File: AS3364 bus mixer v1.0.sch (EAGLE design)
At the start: 62 parts, among them IC1 TL072JD, IC2 TL072JD, IC3 TL072JD, IC30 TL072JT, IC4 TL072JD, IC5 79L09F, IC6 78L09F, IC7 CH446Q

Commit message: Tracing the bus mixer
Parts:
- removed SV1: (no value), joakim:MA15-1JP
- added +12V, -12V, BC_IN, BUS_A, BUS_B, CS/CK, CV1, CV2, CV3, CV4, CV5, CV6, CV7, CV8, DAT, DIST_IN, FX_A, FX_B, GND, IN1, IN2, IN3, IN4, IN5, IN6, IN7, IN8, RST, STB: (no value), joakim:MA01-1JN8MM
- IC1, IC2, IC3, IC4: value TL072JD -> TL072JT; device joakim:TL072JD -> joakim:TL072JT
- R14, R15, R16, R17, R31, R32, R33, R34, R47, R48: device rcl:R-EU_R0603 -> rcl:R-EU_R0402
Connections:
- new net BITCRUSH_IN: BC_IN.1, IC7.Y5
- new net CS/CK: CS/CK.1, IC7.CS/CK
- new net CV5: CV5.1, R19.1
- new net CV6: CV6.1, R20.1
- new net CV6_IN: DA1G$1.CV1, R20.2, R28.2
- new net CV7: CV7.1, R18.1
- new net CV8: CV8.1, R21.1
- new net DAT: DAT.1, IC7.DAT
- new net DIST_IN: DIST_IN.1, IC7.Y4
- new net FX_A: FX_A.1, IC7.Y2
- new net FX_B: FX_B.1, IC7.Y3
- new net IN5: DA1G$1.IN4, IN5.1
- new net IN6: DA1G$1.IN1, IN6.1
- new net IN7: DA1G$1.IN3, IN7.1
- new net IN8: DA1G$1.IN2, IN8.1
- new net OUT5: IC4A.-IN, IC4A.OUT, R34.1
- new net OUT6: IC4B.-IN, IC4B.OUT, R31.1
- new net OUT7: IC3A.-IN, IC3A.OUT, R33.1
- new net OUT8: IC3B.-IN, IC3B.OUT, R32.1
- new net RST: IC7.RST, RST.1
- new net STB: IC7.STB, STB.1
- new net SW1: IC7.X0, R17.2
- new net SW2: IC7.X1, R14.2
- new net SW3: IC7.X2, R16.2
- new net SW4: IC7.X3, R15.2
- new net SW5: IC7.X4, R34.2
- new net SW6: IC7.X5, R31.2
- new net SW7: IC7.X6, R33.2
- new net SW8: IC7.X7, R32.2
- net +12V: now also +12V.1; no longer SV1.14
- net -12V: now also -12V.1; no longer SV1.13
- net BUS_A: now also BUS_A.1, IC7.Y0
- net BUS_B: now also BUS_B.1, IC7.Y1
- net CV1: now also CV1.1; no longer R19.1, SV1.5
- net CV2: now also CV2.1; no longer R20.1, SV1.6
- net CV2_IN: no longer DA1G$1.CV1, R20.2, R28.2
- net CV3: now also CV3.1; no longer R18.1, SV1.7
- net CV4: now also CV4.1; no longer R21.1, SV1.8
- net GND: now also GND.1; no longer SV1.15
- net IN1: now also IN1.1; no longer DA1G$1.IN4, SV1.3
- net IN2: now also IN2.1; no longer DA1G$1.IN1, SV1.4
- net IN3: now also IN3.1; no longer DA1G$1.IN3, SV1.9
- net IN4: now also IN4.1; no longer DA1G$1.IN2, SV1.10
- net OUT1: no longer IC4A.-IN, IC4A.OUT, R34.1, SV1.1
- net OUT2: no longer IC4B.-IN, IC4B.OUT, R31.1, SV1.2
- net OUT3: no longer IC3A.-IN, IC3A.OUT, R33.1, SV1.11
- net OUT4: no longer IC3B.-IN, IC3B.OUT, R32.1, SV1.12
- net SUM_A: now also IC30B.OUT, IC7.X8, R47.2; no longer IC30A.OUT, R48.2
- net SUM_B: now also IC30A.OUT, IC7.X9, R48.2; no longer IC30B.OUT, R47.2
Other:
- moved on the sheet: IC30A, IC30B, R47, R48

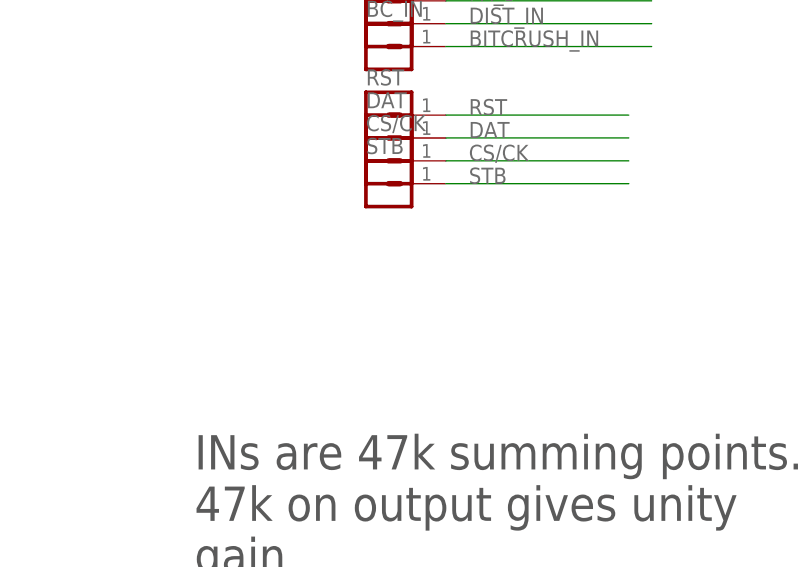
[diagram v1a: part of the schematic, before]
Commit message: Most of lower part traced ok
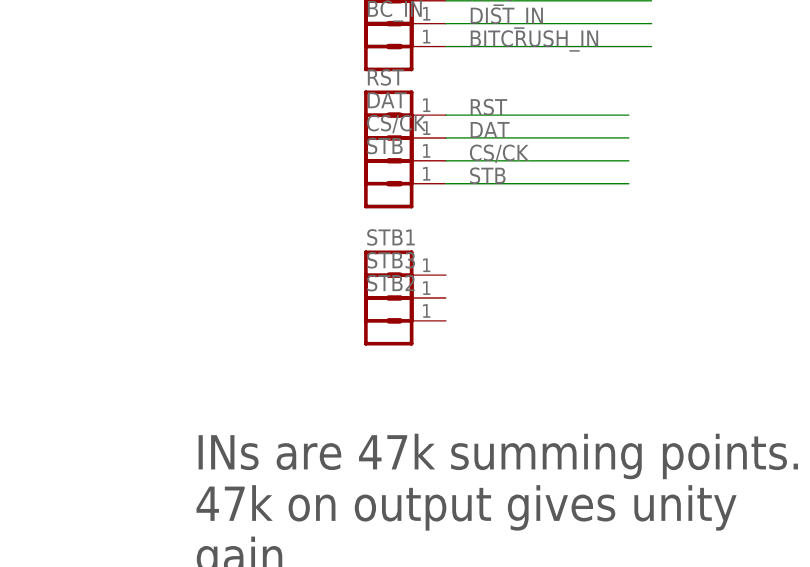
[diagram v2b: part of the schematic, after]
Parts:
- added STB1, STB2, STB3: (no value), joakim:MA01-1JN8MM
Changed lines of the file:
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@@
 <part name="CS/CK" library="joakim" deviceset="MA01-1J" device="N8MM"/>
 <part name="STB" library="joakim" deviceset="MA01-1J" device="N8MM"/>
+<part name="STB1" library="joakim" deviceset="MA01-1J" device="N8MM"/>
+<part name="STB2" library="joakim" deviceset="MA01-1J" device="N8MM"/>
+<part name="STB3" library="joakim" deviceset="MA01-1J" device="N8MM"/>
 </parts>
 <sheets>
@@
 <attribute name="NAME" x="-69.85" y="-6.858" size="1.778" layer="95"/>
 </instance>
+<instance part="STB1" gate="G$1" x="-68.58" y="-20.32" smashed="yes">
+<attribute name="VALUE" x="-69.85" y="-25.4" size="1.778" layer="96"/>
+<attribute name="NAME" x="-69.85" y="-17.018" size="1.778" layer="95"/>
+</instance>
+<instance part="STB2" gate="G$1" x="-68.58" y="-25.4" smashed="yes">
+<attribute name="VALUE" x="-69.85" y="-30.48" size="1.778" layer="96"/>
+<attribute name="NAME" x="-69.85" y="-22.098" size="1.778" layer="95"/>
+</instance>
+<instance part="STB3" gate="G$1" x="-68.58" y="-22.86" smashed="yes">
+<attribute name="VALUE" x="-69.85" y="-27.94" size="1.778" layer="96"/>
+<attribute name="NAME" x="-69.85" y="-19.558" size="1.778" layer="95"/>
+</instance>
 </instances>

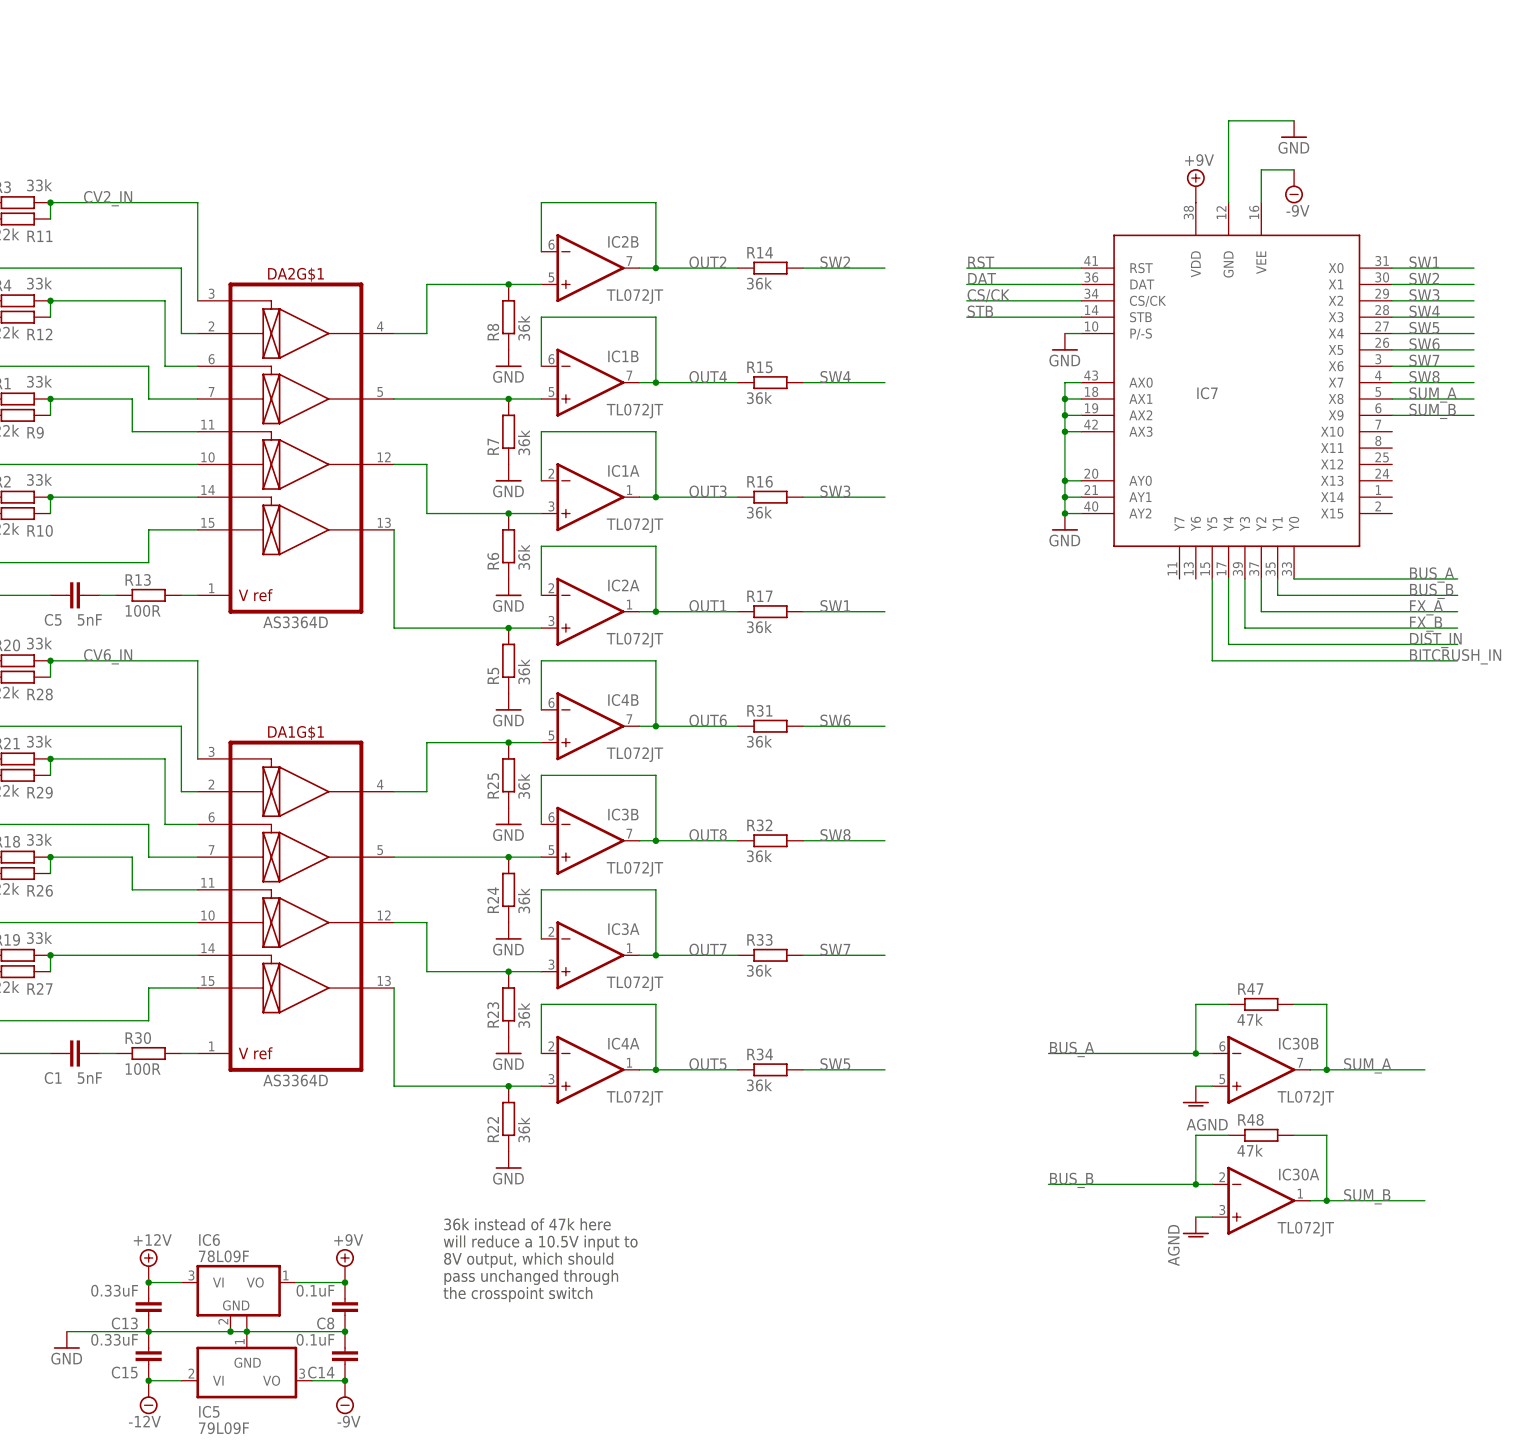
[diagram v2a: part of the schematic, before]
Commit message: Missing 12V to left side only
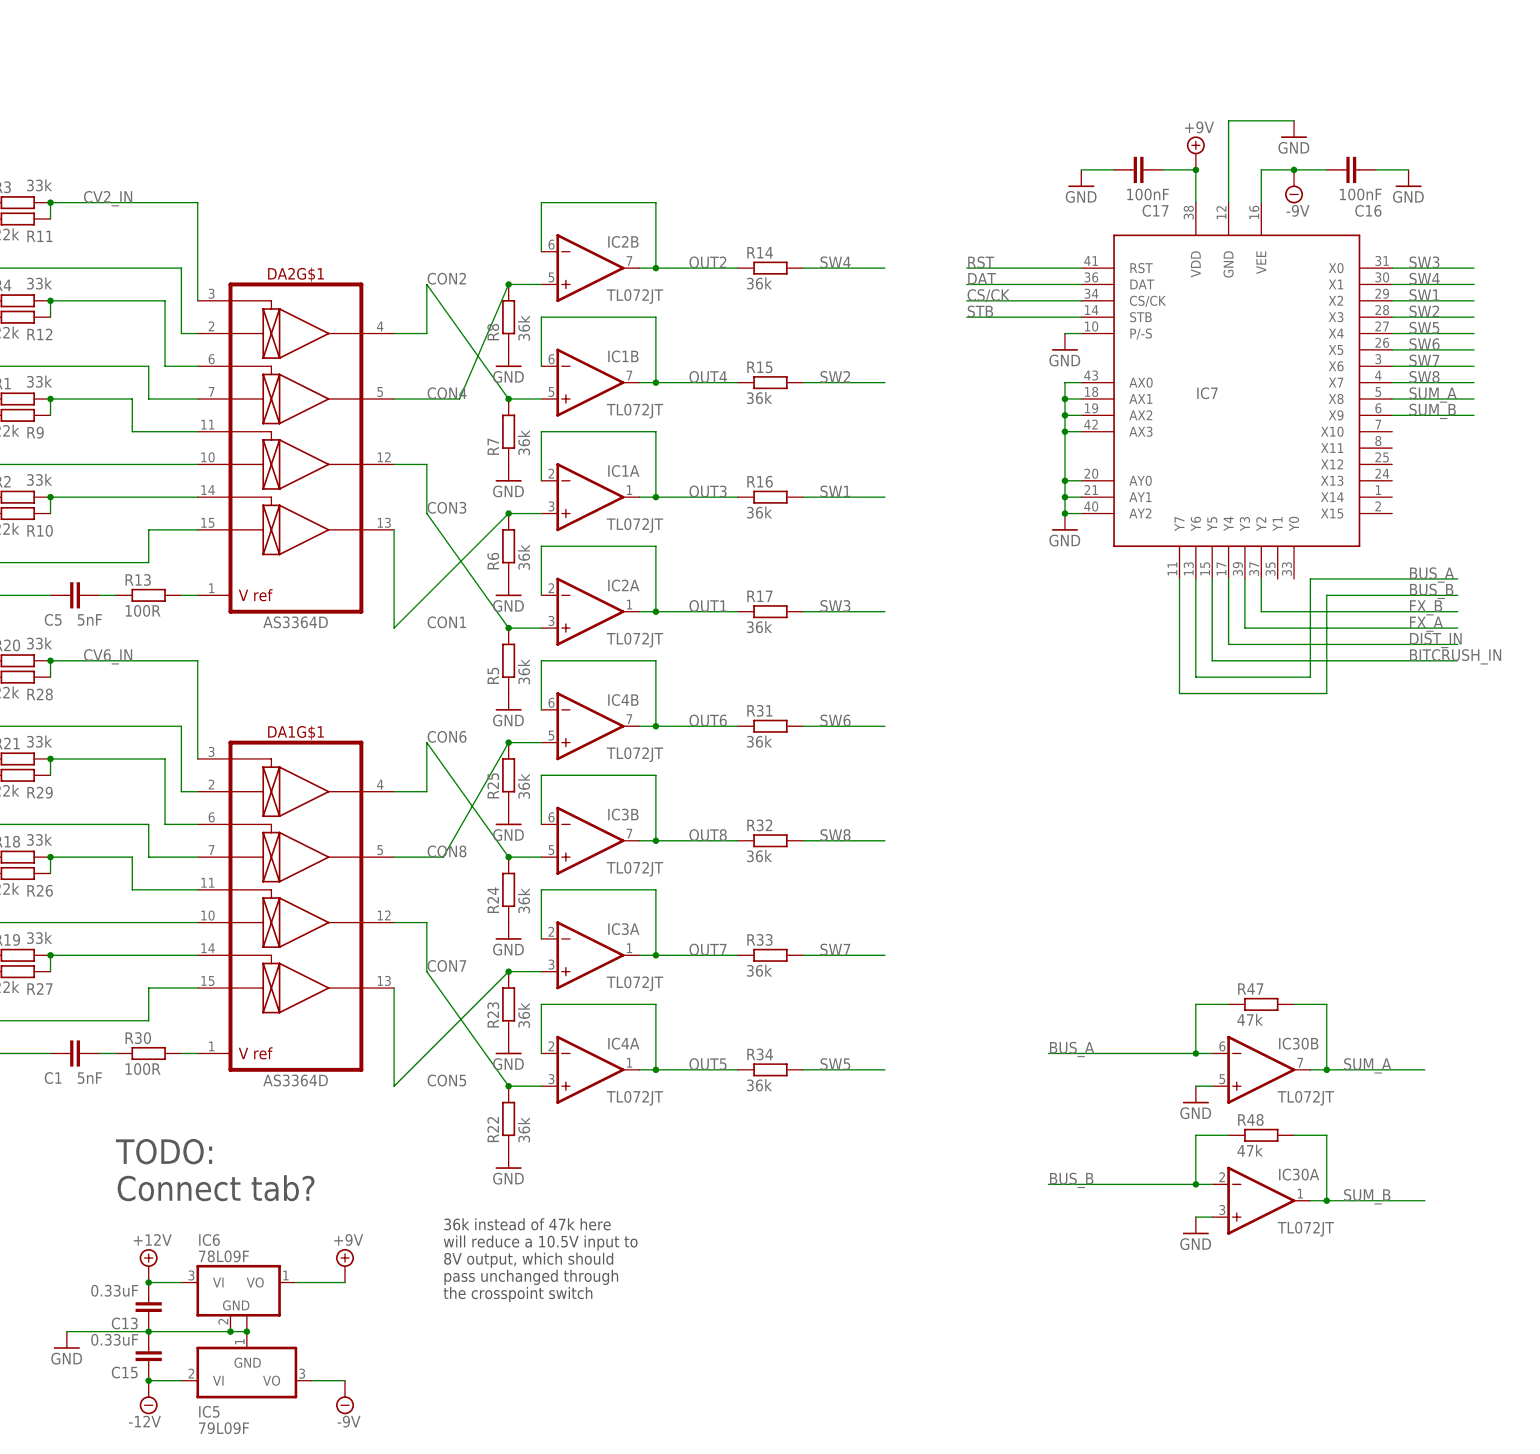
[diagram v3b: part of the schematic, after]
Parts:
- removed C14, C8: 0.1uF, resistor:C-EUC0603
- added C16, C17: 100nF, rcl:C-EUC0402
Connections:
- removed net AGND: IC30A.+IN, IC30B.+IN
- removed net N$11: DA2G$1.OUT3, IC1A.+IN, R6.2
- removed net N$13: DA2G$1.OUT4, IC2A.+IN, R5.2
- removed net N$15: DA1G$1.OUT2, IC3B.+IN, R24.2
- removed net N$16: DA1G$1.OUT3, IC3A.+IN, R23.2
- removed net N$17: DA1G$1.OUT4, IC4A.+IN, R22.2
- removed net N$4: DA2G$1.OUT1, IC2B.+IN, R8.2
- removed net N$6: DA2G$1.OUT2, IC1B.+IN, R7.2
- removed net N$9: DA1G$1.OUT1, IC4B.+IN, R25.2
- new net CON1: DA2G$1.OUT4, IC1A.+IN, R6.2
- new net CON2: DA2G$1.OUT1, IC1B.+IN, R7.2
- new net CON3: DA2G$1.OUT3, IC2A.+IN, R5.2
- new net CON4: DA2G$1.OUT2, IC2B.+IN, R8.2
- new net CON5: DA1G$1.OUT4, IC3A.+IN, R23.2
- new net CON6: DA1G$1.OUT1, IC3B.+IN, R24.2
- new net CON7: DA1G$1.OUT3, IC4A.+IN, R22.2
- new net CON8: DA1G$1.OUT2, IC4B.+IN, R25.2
- net +9V: now also C17.1; no longer C8.2
- net -9V: now also C16.2; no longer C14.1
- net BUS_A: now also IC7.Y6; no longer IC7.Y0
- net BUS_B: now also IC7.Y7; no longer IC7.Y1
- net FX_A: now also IC7.Y3; no longer IC7.Y2
- net FX_B: now also IC7.Y2; no longer IC7.Y3
- net GND: now also C16.1, C17.2, IC30A.+IN, IC30B.+IN; no longer C14.2, C8.1
- net SW1: now also IC7.X2, R16.2; no longer IC7.X0, R17.2
- net SW2: now also IC7.X3, R15.2; no longer IC7.X1, R14.2
- net SW3: now also IC7.X0, R17.2; no longer IC7.X2, R16.2
- net SW4: now also IC7.X1, R14.2; no longer IC7.X3, R15.2
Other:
- note added: "TODO: Connect tab?"
